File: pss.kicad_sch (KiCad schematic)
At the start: 33 parts, among them J1001 Conn_01x02_Socket, J1002 Conn_01x02_Socket, J1003 Conn_01x06_Socket, J1004 Conn_01x02_Socket

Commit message: add pss 3dmodels and testpoints
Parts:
- JP1001: footprint (none) -> pss:SolderJumper-3_P1.3mm_Bridged12-Soldermask-Paste_RoundedPad1.0x1.5mm
- JP1002: footprint (none) -> pss:SolderJumper-2_P1.3mm_Bridged-Soldermask-Paste_RoundedPad1.0x1.5mm
- JP1003, JP1004, JP1005, JP1006, JP1007, JP1008, JP1009, JP1010, JP1011, JP1012, JP1013, JP1014, JP1015, JP1016, JP1017, JP1018, JP1019, JP1020, JP1021, JP1022, JP1023, JP1024, JP1025, JP1026, JP1027, JP1028, JP1029: footprint (none) -> Jumper:SolderJumper-2_P1.3mm_Open_RoundedPad1.0x1.5mm
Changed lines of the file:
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@@
 			)
 		)
-		(property "Footprint" ""
+		(property "Footprint" "Jumper:SolderJumper-2_P1.3mm_Open_RoundedPad1.0x1.5mm"
 			(at 190.5 123.19 0)
 			(effects
@@
 			)
 		)
-		(property "Footprint" ""
+		(property "Footprint" "Jumper:SolderJumper-2_P1.3mm_Open_RoundedPad1.0x1.5mm"
 			(at 168.91 27.94 0)
 			(effects
@@
 			)
 		)
-		(property "Footprint" ""
+		(property "Footprint" "Jumper:SolderJumper-2_P1.3mm_Open_RoundedPad1.0x1.5mm"
 			(at 74.93 144.78 0)
 			(effects
@@
 			)
 		)
-		(property "Footprint" ""
+		(property "Footprint" "Jumper:SolderJumper-2_P1.3mm_Open_RoundedPad1.0x1.5mm"
 			(at 68.58 144.78 0)
 			(effects
@@
 			)
 		)
-		(property "Footprint" ""
+		(property "Footprint" "Jumper:SolderJumper-2_P1.3mm_Open_RoundedPad1.0x1.5mm"
 			(at 168.91 30.48 0)
 			(effects
@@
 			)
 		)
-		(property "Footprint" ""
+		(property "Footprint" "Jumper:SolderJumper-2_P1.3mm_Open_RoundedPad1.0x1.5mm"
 			(at 168.91 48.26 0)
 			(effects
@@
 			)
 		)
-		(property "Footprint" ""
+		(property "Footprint" "Jumper:SolderJumper-2_P1.3mm_Open_RoundedPad1.0x1.5mm"
 			(at 190.5 125.73 0)
 			(effects
@@
 			)
 		)
-		(property "Footprint" ""
+		(property "Footprint" "Jumper:SolderJumper-2_P1.3mm_Open_RoundedPad1.0x1.5mm"
 			(at 77.47 144.78 0)
 			(effects
@@
 			)
 		)
-		(property "Footprint" ""
+		(property "Footprint" "Jumper:SolderJumper-2_P1.3mm_Open_RoundedPad1.0x1.5mm"
 			(at 63.5 144.78 0)
 			(effects
@@
 			)
 		)
-		(property "Footprint" ""
+		(property "Footprint" "Jumper:SolderJumper-2_P1.3mm_Open_RoundedPad1.0x1.5mm"
 			(at 93.98 27.94 0)
 			(effects
@@
 			)
 		)
-		(property "Footprint" ""
+		(property "Footprint" "Jumper:SolderJumper-2_P1.3mm_Open_RoundedPad1.0x1.5mm"
 			(at 93.98 33.02 0)
 			(effects
@@
 			)
 		)
-		(property "Footprint" ""
+		(property "Footprint" "Jumper:SolderJumper-2_P1.3mm_Open_RoundedPad1.0x1.5mm"
 			(at 168.91 45.72 0)
 			(effects
@@
 			)
 		)
-		(property "Footprint" ""
+		(property "Footprint" "Jumper:SolderJumper-2_P1.3mm_Open_RoundedPad1.0x1.5mm"
 			(at 72.39 144.78 0)
 			(effects
@@
 			)
 		)
-		(property "Footprint" ""
+		(property "Footprint" "Jumper:SolderJumper-2_P1.3mm_Open_RoundedPad1.0x1.5mm"
 			(at 168.91 39.37 0)
 			(effects
@@
 			)
 		)
-		(property "Footprint" ""
+		(property "Footprint" "Jumper:SolderJumper-2_P1.3mm_Open_RoundedPad1.0x1.5mm"
 			(at 154.94 120.65 0)
 			(effects
@@
 			)
 		)
-		(property "Footprint" ""
+		(property "Footprint" "Jumper:SolderJumper-2_P1.3mm_Open_RoundedPad1.0x1.5mm"
 			(at 125.73 120.65 0)
 			(effects
@@
 			)
 		)
-		(property "Footprint" ""
+		(property "Footprint" "Jumper:SolderJumper-2_P1.3mm_Open_RoundedPad1.0x1.5mm"
 			(at 168.91 33.02 0)
 			(effects
@@
 			)
 		)
-		(property "Footprint" ""
+		(property "Footprint" "Jumper:SolderJumper-2_P1.3mm_Open_RoundedPad1.0x1.5mm"
 			(at 168.91 52.07 0)
 			(effects
@@
 			)
 		)
-		(property "Footprint" ""
+		(property "Footprint" "pss:SolderJumper-3_P1.3mm_Bridged12-Soldermask-Paste_RoundedPad1.0x1.5mm"
 			(at 139.7 40.64 0)
 			(effects
@@
 			)
 		)
-		(property "Footprint" ""
+		(property "Footprint" "Jumper:SolderJumper-2_P1.3mm_Open_RoundedPad1.0x1.5mm"
 			(at 168.91 41.91 0)
 			(effects
@@
 			)
 		)
-		(property "Footprint" ""
+		(property "Footprint" "Jumper:SolderJumper-2_P1.3mm_Open_RoundedPad1.0x1.5mm"
 			(at 96.52 119.38 0)
 			(effects
@@
 			)
 		)
-		(property "Footprint" ""
+		(property "Footprint" "Jumper:SolderJumper-2_P1.3mm_Open_RoundedPad1.0x1.5mm"
 			(at 96.52 121.92 0)
 			(effects
@@
 			)
 		)
-		(property "Footprint" ""
+		(property "Footprint" "Jumper:SolderJumper-2_P1.3mm_Open_RoundedPad1.0x1.5mm"
 			(at 93.98 30.48 0)
 			(effects
@@
 			)
 		)
-		(property "Footprint" ""
+		(property "Footprint" "Jumper:SolderJumper-2_P1.3mm_Open_RoundedPad1.0x1.5mm"
 			(at 168.91 36.83 0)
 			(effects
@@
 			)
 		)
-		(property "Footprint" ""
+		(property "Footprint" "Jumper:SolderJumper-2_P1.3mm_Open_RoundedPad1.0x1.5mm"
 			(at 93.98 35.56 0)
 			(effects
@@
 			)
 		)
-		(property "Footprint" ""
+		(property "Footprint" "Jumper:SolderJumper-2_P1.3mm_Open_RoundedPad1.0x1.5mm"
 			(at 66.04 144.78 0)
 			(effects
@@
 			)
 		)
-		(property "Footprint" ""
+		(property "Footprint" "Jumper:SolderJumper-2_P1.3mm_Open_RoundedPad1.0x1.5mm"
 			(at 168.91 54.61 0)
 			(effects
@@
 			)
 		)
-		(property "Footprint" ""
+		(property "Footprint" "Jumper:SolderJumper-2_P1.3mm_Open_RoundedPad1.0x1.5mm"
 			(at 190.5 120.65 0)
 			(effects
@@
 			)
 		)
-		(property "Footprint" ""
+		(property "Footprint" "pss:SolderJumper-2_P1.3mm_Bridged-Soldermask-Paste_RoundedPad1.0x1.5mm"
 			(at 134.62 88.9 0)
 			(effects

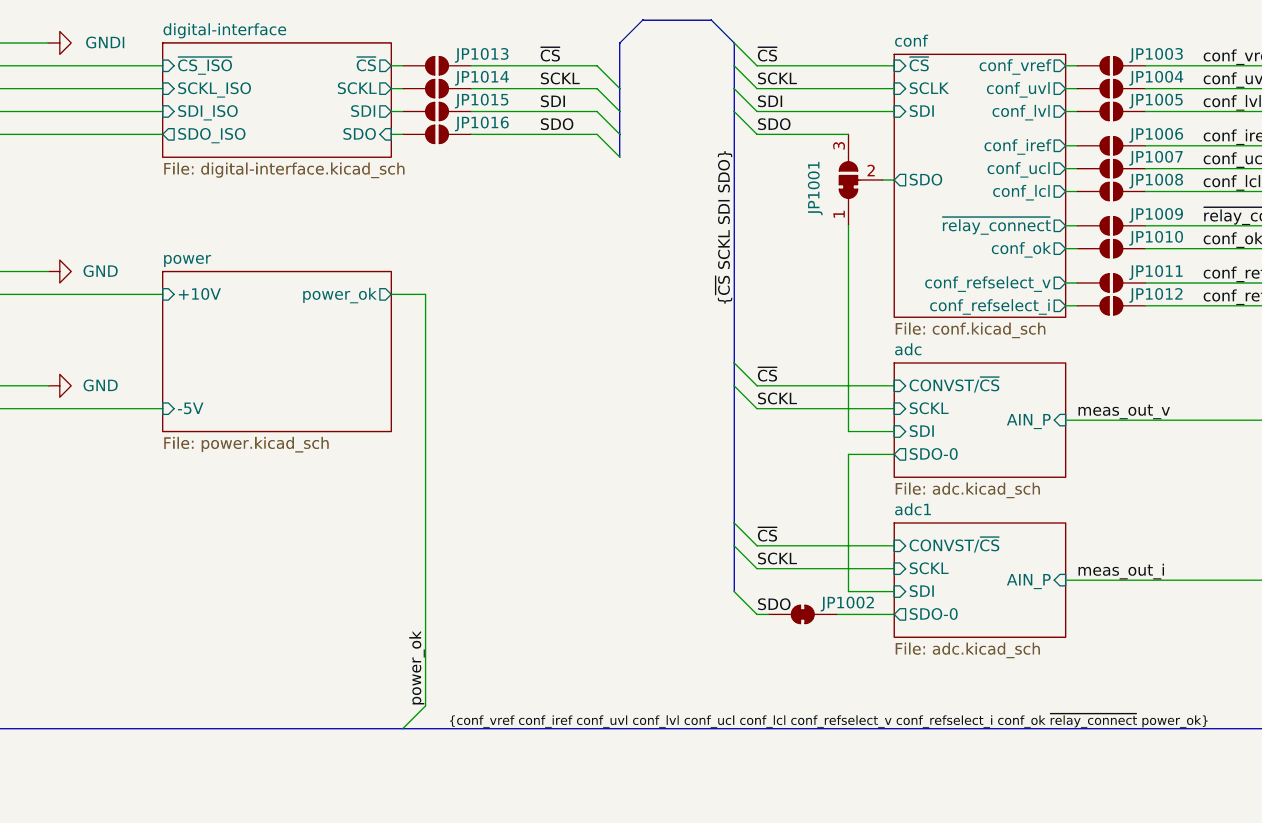
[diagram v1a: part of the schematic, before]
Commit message: edit pss alphabetically order pages
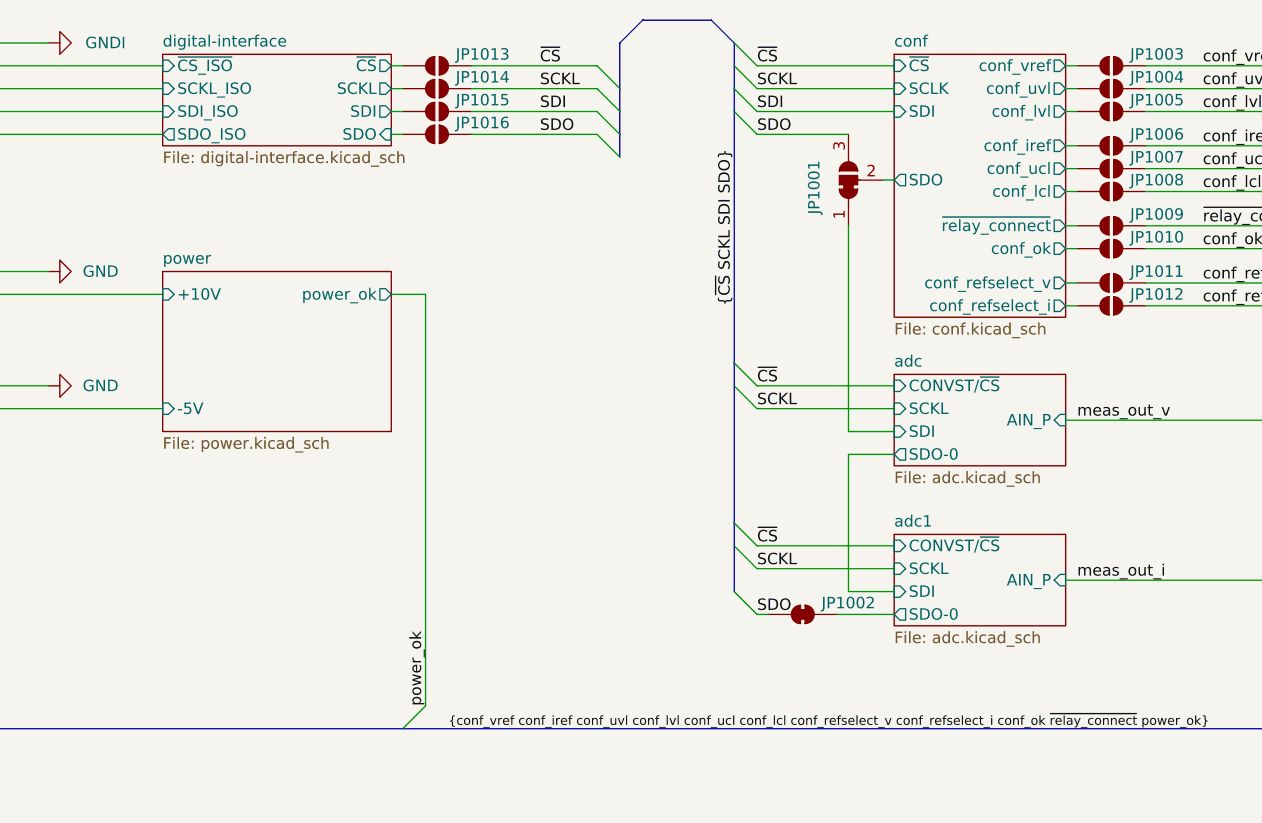
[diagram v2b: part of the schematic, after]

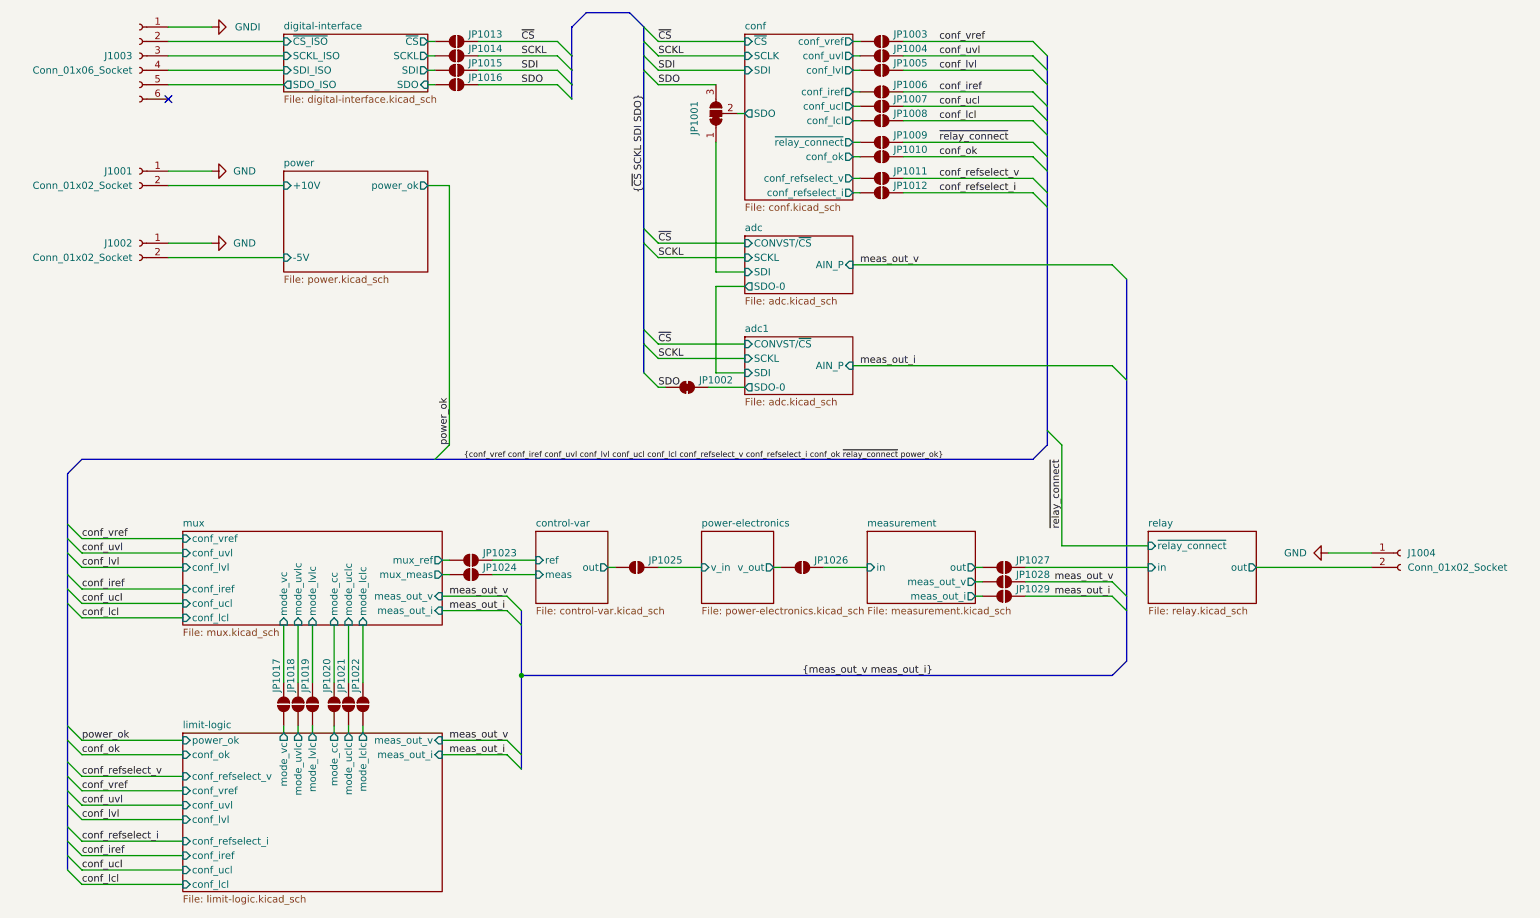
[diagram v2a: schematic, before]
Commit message: edit pss reannotate entire schematic
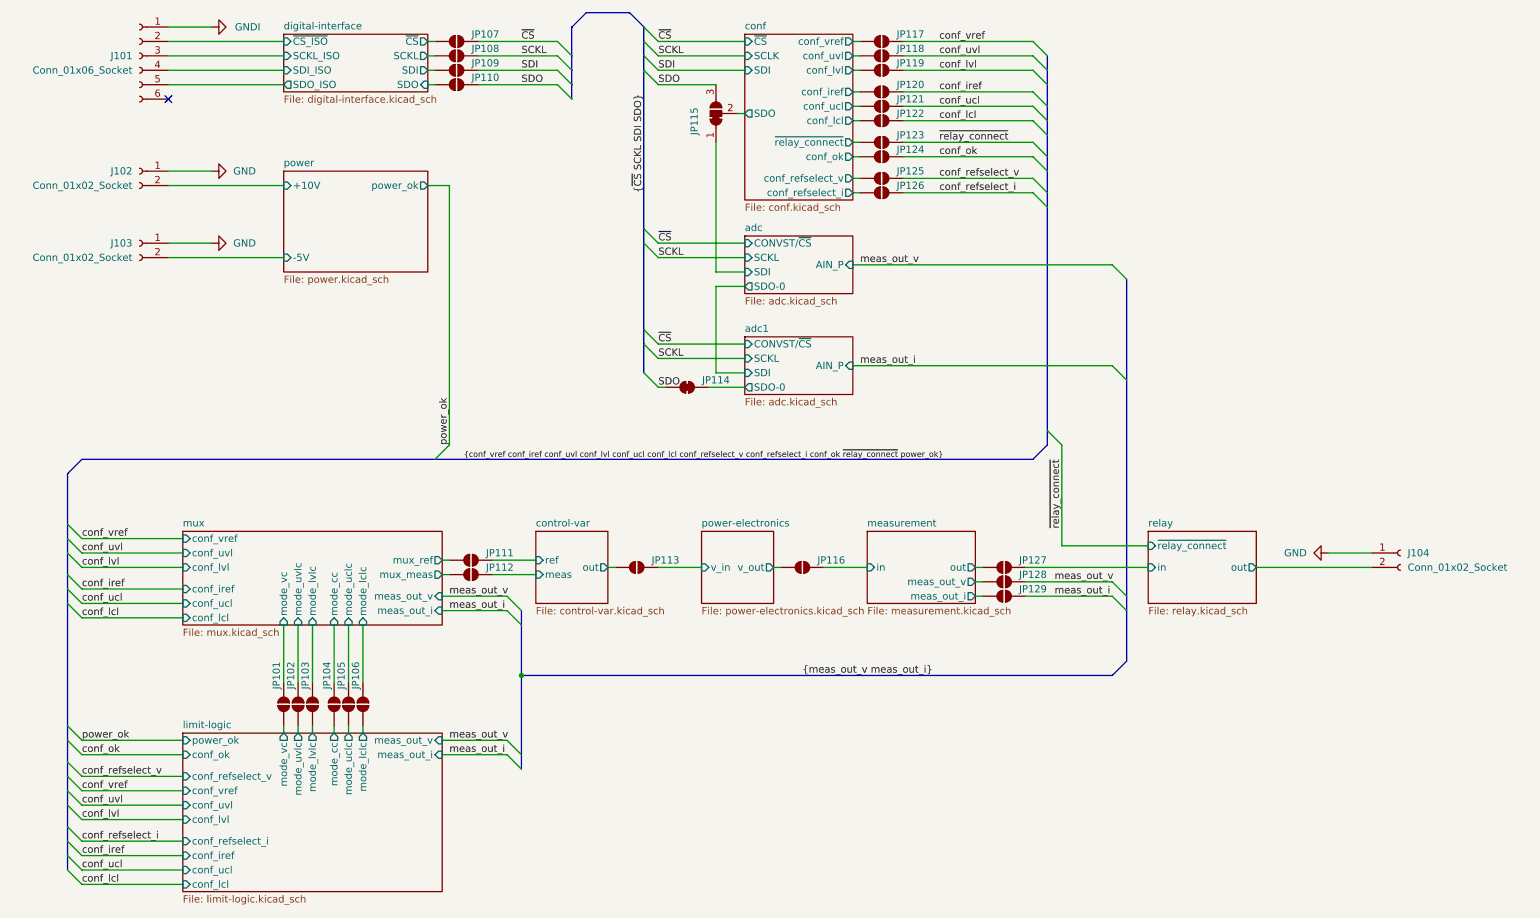
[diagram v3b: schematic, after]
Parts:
- renumbered J1003 to J101, J1001 to J102, J1002 to J103, J1004 to J104, JP1017 to JP101, JP1018 to JP102, JP1019 to JP103, JP1020 to JP104, JP1021 to JP105, JP1022 to JP106, JP1013 to JP107, JP1014 to JP108, JP1015 to JP109, JP1016 to JP110, JP1023 to JP111, JP1024 to JP112, JP1025 to JP113, JP1002 to JP114, JP1001 to JP115, JP1026 to JP116, JP1003 to JP117, JP1004 to JP118, JP1005 to JP119, JP1006 to JP120, JP1007 to JP121, JP1008 to JP122, JP1009 to JP123, JP1010 to JP124, JP1011 to JP125, JP1012 to JP126, JP1027 to JP127, JP1028 to JP128, JP1029 to JP129

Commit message: edit pss symbol library: export all schematic symbols to library 'pss' and update symbol link
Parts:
- J101: symbol Connector:Conn_01x06_Socket -> pss:Conn_01x06_Socket
- J102, J103, J104: symbol Connector:Conn_01x02_Socket -> pss:Conn_01x02_Socket
- JP101, JP102, JP103, JP104, JP105, JP106, JP107, JP108, JP109, JP110, JP111, JP112, JP113, JP116, JP117, JP118, JP119, JP120, JP121, JP122, JP123, JP124, JP125, JP126, JP127, JP128, JP129: symbol Jumper:SolderJumper_2_Open -> pss:SolderJumper_2_Open
- JP114: symbol Jumper:SolderJumper_2_Bridged -> pss:SolderJumper_2_Bridged
- JP115: symbol Jumper:SolderJumper_3_Bridged12 -> pss:SolderJumper_3_Bridged12
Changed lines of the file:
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@@
 	)
 	(symbol
-		(lib_id "Jumper:SolderJumper_2_Open")
+		(lib_id "pss:SolderJumper_2_Open")
 		(at 190.5 123.19 0)
 		(unit 1)
@@
 	)
 	(symbol
-		(lib_id "Jumper:SolderJumper_2_Open")
+		(lib_id "pss:SolderJumper_2_Open")
 		(at 168.91 27.94 0)
 		(unit 1)
@@
 	)
 	(symbol
-		(lib_id "Jumper:SolderJumper_2_Open")
+		(lib_id "pss:SolderJumper_2_Open")
 		(at 74.93 144.78 90)
 		(unit 1)
@@
 	)
 	(symbol
-		(lib_id "Jumper:SolderJumper_2_Open")
+		(lib_id "pss:SolderJumper_2_Open")
 		(at 68.58 144.78 90)
 		(unit 1)
@@
 	)
 	(symbol
-		(lib_id "Connector:Conn_01x02_Socket")
+		(lib_id "pss:Conn_01x02_Socket")
 		(at 260.35 118.11 0)
 		(unit 1)
@@
 	)
 	(symbol
-		(lib_id "Jumper:SolderJumper_2_Open")
+		(lib_id "pss:SolderJumper_2_Open")
 		(at 168.91 30.48 0)
 		(unit 1)
@@
 	)
 	(symbol
-		(lib_id "Jumper:SolderJumper_2_Open")
+		(lib_id "pss:SolderJumper_2_Open")
 		(at 168.91 48.26 0)
 		(unit 1)
@@
 	)
 	(symbol
-		(lib_id "Jumper:SolderJumper_2_Open")
+		(lib_id "pss:SolderJumper_2_Open")
 		(at 190.5 125.73 0)
 		(unit 1)
@@
 	)
 	(symbol
-		(lib_id "Jumper:SolderJumper_2_Open")
+		(lib_id "pss:SolderJumper_2_Open")
 		(at 77.47 144.78 90)
 		(unit 1)
@@
 	)
 	(symbol
-		(lib_id "Connector:Conn_01x02_Socket")
+		(lib_id "pss:Conn_01x02_Socket")
 		(at 38.1 63.5 0)
 		(mirror y)
@@
 	)
 	(symbol
-		(lib_id "Jumper:SolderJumper_2_Open")
+		(lib_id "pss:SolderJumper_2_Open")
 		(at 63.5 144.78 90)
 		(unit 1)
@@
 	)
 	(symbol
-		(lib_id "Jumper:SolderJumper_2_Open")
+		(lib_id "pss:SolderJumper_2_Open")
 		(at 93.98 27.94 0)
 		(unit 1)
@@
 	)
 	(symbol
-		(lib_id "Jumper:SolderJumper_2_Open")
+		(lib_id "pss:SolderJumper_2_Open")
 		(at 93.98 33.02 0)
 		(unit 1)
@@
 	)
 	(symbol
-		(lib_id "Jumper:SolderJumper_2_Open")
+		(lib_id "pss:SolderJumper_2_Open")
 		(at 168.91 45.72 0)
 		(unit 1)
@@
 	)
 	(symbol
-		(lib_id "Jumper:SolderJumper_2_Open")
+		(lib_id "pss:SolderJumper_2_Open")
 		(at 72.39 144.78 90)
 		(unit 1)
@@
 	)
 	(symbol
-		(lib_id "Jumper:SolderJumper_2_Open")
+		(lib_id "pss:SolderJumper_2_Open")
 		(at 168.91 39.37 0)
 		(unit 1)
@@
 	)
 	(symbol
-		(lib_id "Jumper:SolderJumper_2_Open")
+		(lib_id "pss:SolderJumper_2_Open")
 		(at 154.94 120.65 0)
 		(unit 1)
@@
 	)
 	(symbol
-		(lib_id "Jumper:SolderJumper_2_Open")
+		(lib_id "pss:SolderJumper_2_Open")
 		(at 125.73 120.65 0)
 		(unit 1)
@@
 	)
 	(symbol
-		(lib_id "Connector:Conn_01x06_Socket")
+		(lib_id "pss:Conn_01x06_Socket")
 		(at 38.1 30.48 0)
 		(mirror y)
@@
 	)
 	(symbol
-		(lib_id "Jumper:SolderJumper_2_Open")
+		(lib_id "pss:SolderJumper_2_Open")
 		(at 168.91 33.02 0)
 		(unit 1)
@@
 	)
 	(symbol
-		(lib_id "Jumper:SolderJumper_2_Open")
+		(lib_id "pss:SolderJumper_2_Open")
 		(at 168.91 52.07 0)
 		(unit 1)
@@
 	)
 	(symbol
-		(lib_id "Jumper:SolderJumper_3_Bridged12")
+		(lib_id "pss:SolderJumper_3_Bridged12")
 		(at 139.7 40.64 90)
 		(unit 1)
@@
 	)
 	(symbol
-		(lib_id "Connector:Conn_01x02_Socket")
+		(lib_id "pss:Conn_01x02_Socket")
 		(at 38.1 50.8 0)
 		(mirror y)
@@
 	)
 	(symbol
-		(lib_id "Jumper:SolderJumper_2_Open")
+		(lib_id "pss:SolderJumper_2_Open")
 		(at 168.91 41.91 0)
 		(unit 1)
@@
 	)
 	(symbol
-		(lib_id "Jumper:SolderJumper_2_Open")
+		(lib_id "pss:SolderJumper_2_Open")
 		(at 96.52 119.38 0)
 		(unit 1)
@@
 	)
 	(symbol
-		(lib_id "Jumper:SolderJumper_2_Open")
+		(lib_id "pss:SolderJumper_2_Open")
 		(at 96.52 121.92 0)
 		(unit 1)
@@
 	)
 	(symbol
-		(lib_id "Jumper:SolderJumper_2_Open")
+		(lib_id "pss:SolderJumper_2_Open")
 		(at 93.98 30.48 0)
 		(unit 1)
@@
 	)
 	(symbol
-		(lib_id "Jumper:SolderJumper_2_Open")
+		(lib_id "pss:SolderJumper_2_Open")
 		(at 168.91 36.83 0)
 		(unit 1)
@@
 	)
 	(symbol
-		(lib_id "Jumper:SolderJumper_2_Open")
+		(lib_id "pss:SolderJumper_2_Open")
 		(at 93.98 35.56 0)
 		(unit 1)
@@
 	)
 	(symbol
-		(lib_id "Jumper:SolderJumper_2_Open")
+		(lib_id "pss:SolderJumper_2_Open")
 		(at 66.04 144.78 90)
 		(unit 1)
@@
 	)
 	(symbol
-		(lib_id "Jumper:SolderJumper_2_Open")
+		(lib_id "pss:SolderJumper_2_Open")
 		(at 168.91 54.61 0)
 		(unit 1)
@@
 	)
 	(symbol
-		(lib_id "Jumper:SolderJumper_2_Open")
+		(lib_id "pss:SolderJumper_2_Open")
 		(at 190.5 120.65 0)
 		(unit 1)
@@
 	)
 	(symbol
-		(lib_id "Jumper:SolderJumper_2_Bridged")
+		(lib_id "pss:SolderJumper_2_Bridged")
 		(at 134.62 88.9 180)
 		(unit 1)
